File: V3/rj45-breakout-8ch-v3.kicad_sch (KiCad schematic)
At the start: 13 parts, among them J1 Jack RJ45, J10 Conn_01x06, J11 Conn_01x06, J12 Conn_01x06, J13 Conn_01x06, J2 Jack RJ45, J3 Jack RJ45, J4 Jack RJ45, J5 Jack RJ45, J6 Jack RJ45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

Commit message: Part numbers update
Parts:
- J1, J2, J3, J4, J5, J6, J7, J8: JLCPCB BOM (none) -> 0
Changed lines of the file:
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@@
       (effects (font (size 1.27 1.27)) hide)
     )
-    (property "JLCPCB BOM" "~" (at 77.47 140.97 0)
+    (property "JLCPCB BOM" "0" (at 77.47 140.97 0)
       (effects (font (size 1.27 1.27)) hide)
     )
@@
       (effects (font (size 1.27 1.27)) hide)
     )
-    (property "JLCPCB BOM" "~" (at 77.47 110.49 0)
+    (property "JLCPCB BOM" "0" (at 77.47 110.49 0)
       (effects (font (size 1.27 1.27)) hide)
     )
@@
       (effects (font (size 1.27 1.27)) hide)
     )
-    (property "JLCPCB BOM" "~" (at 77.47 80.01 0)
+    (property "JLCPCB BOM" "0" (at 77.47 80.01 0)
       (effects (font (size 1.27 1.27)) hide)
     )
@@
       (effects (font (size 1.27 1.27)) hide)
     )
-    (property "JLCPCB BOM" "~" (at 77.47 49.53 0)
+    (property "JLCPCB BOM" "0" (at 77.47 49.53 0)
       (effects (font (size 1.27 1.27)) hide)
     )
@@
       (effects (font (size 1.27 1.27)) hide)
     )
-    (property "JLCPCB BOM" "~" (at 176.53 140.97 0)
+    (property "JLCPCB BOM" "0" (at 176.53 140.97 0)
       (effects (font (size 1.27 1.27)) hide)
     )
@@
       (effects (font (size 1.27 1.27)) hide)
     )
-    (property "JLCPCB BOM" "~" (at 176.53 110.49 0)
+    (property "JLCPCB BOM" "0" (at 176.53 110.49 0)
       (effects (font (size 1.27 1.27)) hide)
     )
@@
       (effects (font (size 1.27 1.27)) hide)
     )
-    (property "JLCPCB BOM" "~" (at 176.53 80.01 0)
+    (property "JLCPCB BOM" "0" (at 176.53 80.01 0)
       (effects (font (size 1.27 1.27)) hide)
     )
@@
       (effects (font (size 1.27 1.27)) hide)
     )
-    (property "JLCPCB BOM" "~" (at 176.53 49.53 0)
-      (effects (font (size 1.27 1.27)) hide)
-    )
+    (property "JLCPCB BOM" "0" (at 176.53 49.53 0)
+      (effects (font (size 1.27 1.27)) hide)
+    )

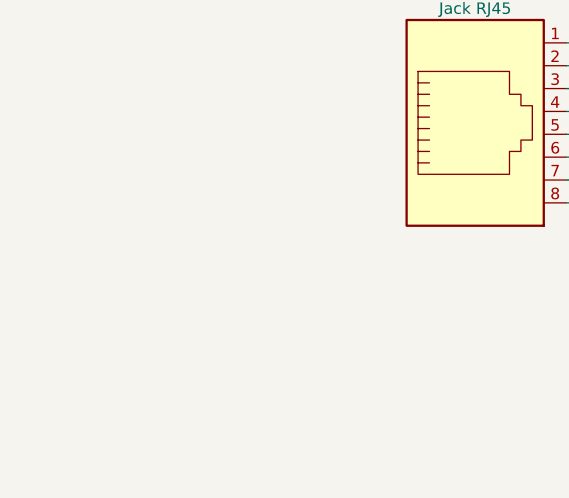
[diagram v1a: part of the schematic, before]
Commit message: Added information on RJ45 connectors
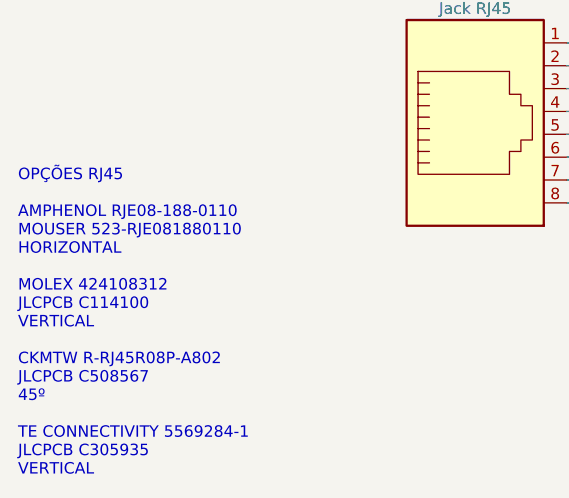
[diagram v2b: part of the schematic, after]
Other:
- note added: "OPÇÕES RJ45 AMPHENOL RJE08-188-0110 MOUSER 523-RJE081880110 HORIZONTAL MOLEX 424108312 JLCPCB C114100 VERTICAL CKMTW R-RJ45R08P-A802 JLCPCB C508567 45º TE CONNECTIVITY 5569284-1 JLCPCB C305935 VERTICAL"
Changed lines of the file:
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@@
     (stroke (width 0) (type default))
+  )
+  (text "OPÇÕES RJ45\n\nAMPHENOL RJE08-188-0110\nMOUSER 523-RJE081880110\nHORIZONTAL\n\nMOLEX 424108312\nJLCPCB C114100\nVERTICAL\n\nCKMTW R-RJ45R08P-A802\nJLCPCB C508567\n45º\n\nTE CONNECTIVITY 5569284-1\nJLCPCB C305935\nVERTICAL"
+    (at 26.67 181.61 0)
+    (effects (font (size 1.27 1.27)) (justify left bottom))
   )
   (symbol (lib_id "Connector:RJ45") (at 77.47 140.97 0) (mirror x) (unit 1)

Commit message: Connectors rotated 180deg
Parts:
- J10, J11, J12, J13: footprint Tales:TerminalBlock_DG141V-2.54-6P_1x06_P2.54mm_Vertical -> Tales:TerminalBlock_Phoenix_FFKDSA1-V-2.54-6_1x06_P2.54mm_Vertical
- J9: footprint Tales:TerminalBlock_JL142V-5.08-2P_1x02_P5.08mm_Vertical -> Tales:TerminalBlock_Phoenix_FFKDSA-V1-5.08-2_1x02_P5.08mm_Vertical
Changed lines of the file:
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@@
       (effects (font (size 1.27 1.27)) (justify left))
     )
-    (property "Footprint" "Tales:TerminalBlock_DG141V-2.54-6P_1x06_P2.54mm_Vertical" (at 212.09 64.77 0)
+    (property "Footprint" "Tales:TerminalBlock_Phoenix_FFKDSA1-V-2.54-6_1x06_P2.54mm_Vertical" (at 212.09 64.77 0)
       (effects (font (size 1.27 1.27)) hide)
     )
@@
       (effects (font (size 1.27 1.27)) (justify left))
     )
-    (property "Footprint" "Tales:TerminalBlock_DG141V-2.54-6P_1x06_P2.54mm_Vertical" (at 113.03 125.73 0)
+    (property "Footprint" "Tales:TerminalBlock_Phoenix_FFKDSA1-V-2.54-6_1x06_P2.54mm_Vertical" (at 113.03 125.73 0)
       (effects (font (size 1.27 1.27)) hide)
     )
@@
       (effects (font (size 1.27 1.27)) (justify left))
     )
-    (property "Footprint" "Tales:TerminalBlock_JL142V-5.08-2P_1x02_P5.08mm_Vertical" (at 113.03 29.21 0)
+    (property "Footprint" "Tales:TerminalBlock_Phoenix_FFKDSA-V1-5.08-2_1x02_P5.08mm_Vertical" (at 113.03 29.21 0)
       (effects (font (size 1.27 1.27)) hide)
     )
@@
       (effects (font (size 1.27 1.27)) (justify left))
     )
-    (property "Footprint" "Tales:TerminalBlock_DG141V-2.54-6P_1x06_P2.54mm_Vertical" (at 113.03 64.77 0)
+    (property "Footprint" "Tales:TerminalBlock_Phoenix_FFKDSA1-V-2.54-6_1x06_P2.54mm_Vertical" (at 113.03 64.77 0)
       (effects (font (size 1.27 1.27)) hide)
     )
@@
       (effects (font (size 1.27 1.27)) (justify left))
     )
-    (property "Footprint" "Tales:TerminalBlock_DG141V-2.54-6P_1x06_P2.54mm_Vertical" (at 212.09 125.73 0)
+    (property "Footprint" "Tales:TerminalBlock_Phoenix_FFKDSA1-V-2.54-6_1x06_P2.54mm_Vertical" (at 212.09 125.73 0)
       (effects (font (size 1.27 1.27)) hide)
     )

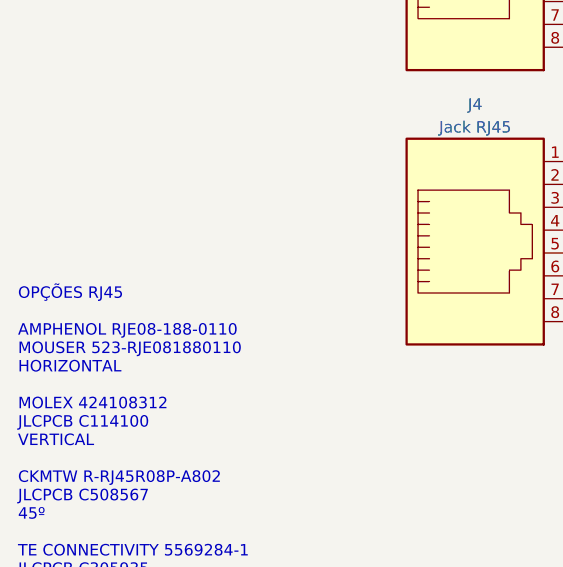
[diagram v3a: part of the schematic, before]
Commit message: Added text regarding RJ45 connectors
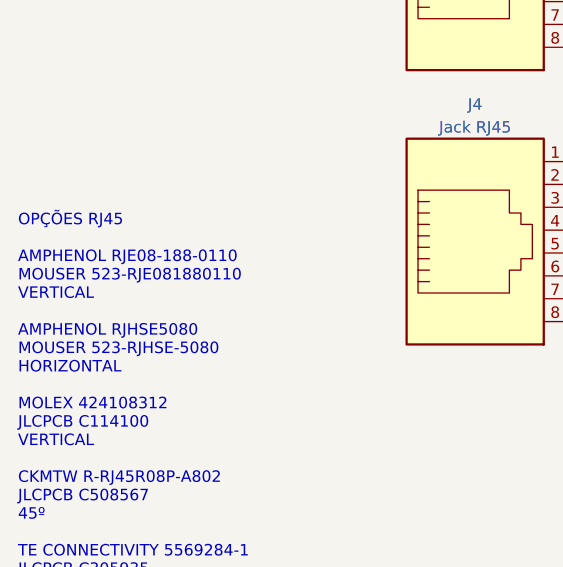
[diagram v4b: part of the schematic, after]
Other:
- note added: "OPÇÕES RJ45 AMPHENOL RJE08-188-0110 MOUSER 523-RJE081880110 VERTICAL AMPHENOL RJHSE5080 MOUSER 523-RJHSE-5080 HORIZONTAL MOLEX 424108312 JLCPCB C114100 VERTICAL CKMTW R-RJ45R08P-A802 JLCPCB C508567 45º TE CONNECTIVITY 5569284-1 JLCPCB C305935 VERTICAL"
- note removed: "OPÇÕES RJ45 AMPHENOL RJE08-188-0110 MOUSER 523-RJE081880110 HORIZONTAL MOLEX 424108312 JLCPCB C114100 VERTICAL CKMTW R-RJ45R08P-A802 JLCPCB C508567 45º TE CONNECTIVITY 5569284-1 JLCPCB C305935 VERTICAL"
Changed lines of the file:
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@@
     (stroke (width 0) (type default))
   )
-  (text "OPÇÕES RJ45\n\nAMPHENOL RJE08-188-0110\nMOUSER 523-RJE081880110\nHORIZONTAL\n\nMOLEX 424108312\nJLCPCB C114100\nVERTICAL\n\nCKMTW R-RJ45R08P-A802\nJLCPCB C508567\n45º\n\nTE CONNECTIVITY 5569284-1\nJLCPCB C305935\nVERTICAL"
+  (text "OPÇÕES RJ45\n\nAMPHENOL RJE08-188-0110\nMOUSER 523-RJE081880110\nVERTICAL\n\nAMPHENOL RJHSE5080\nMOUSER 523-RJHSE-5080\nHORIZONTAL\n\nMOLEX 424108312\nJLCPCB C114100\nVERTICAL\n\nCKMTW R-RJ45R08P-A802\nJLCPCB C508567\n45º\n\nTE CONNECTIVITY 5569284-1\nJLCPCB C305935\nVERTICAL"
     (at 26.67 181.61 0)
     (effects (font (size 1.27 1.27)) (justify left bottom))

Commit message: Layout tweakings
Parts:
- added FID1, FID2, FID3, FID4: Fiducial, Fiducial:Fiducial_1mm_Mask2mm, symbol Mechanical:Fiducial
- J1, J2, J3, J4, J5, J6, J7, J8: JLCPCB BOM 0 -> 1; LCSC Part (none) -> C2902702; Mfr Amphenol -> Ckmtw(Shenzhen Cankemeng); Mfr PN RJE08-188-0110 -> R-RJ45S08P-A004; Vendor Mouser -> JLCPCB; Vendor PN 523-RJE081880110 -> C2902702
- J10: value Conn_01x06 -> SWITCHES1; footprint Tales:TerminalBlock_Phoenix_FFKDSA1-V-2.54-6_1x06_P2.54mm_Vertical -> Tales:TerminalBlock_DB141V-2.54-6P_1x06_P2.54mm_Vertical
- J11: value Conn_01x06 -> SWITCHES2; footprint Tales:TerminalBlock_Phoenix_FFKDSA1-V-2.54-6_1x06_P2.54mm_Vertical -> Tales:TerminalBlock_DB141V-2.54-6P_1x06_P2.54mm_Vertical
- J12: value Conn_01x06 -> SWITCHES3; footprint Tales:TerminalBlock_Phoenix_FFKDSA1-V-2.54-6_1x06_P2.54mm_Vertical -> Tales:TerminalBlock_DB141V-2.54-6P_1x06_P2.54mm_Vertical
- J13: value Conn_01x06 -> SWITCHES4; footprint Tales:TerminalBlock_Phoenix_FFKDSA1-V-2.54-6_1x06_P2.54mm_Vertical -> Tales:TerminalBlock_DB141V-2.54-6P_1x06_P2.54mm_Vertical
- J9: value Conn_01x02 -> 24V; footprint Tales:TerminalBlock_Phoenix_FFKDSA-V1-5.08-2_1x02_P5.08mm_Vertical -> Tales:TerminalBlock_DB142V-2-5.08_1x02_P5.08mm_Vertical; LCSC Part C409160 -> C2898699; Mfr JILN -> DIBO; Mfr PN JL142V-50802GA1 -> DB142V-5.08-2P; Vendor PN C409160 -> C2898699
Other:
- note added: "OPÇÕES RJ45 AMPHENOL RJE08-188-0110 MOUSER 523-RJE081880110 CKMTW(Shenzhen Cankemeng) R-RJ45S08P-A004 JLCPCB C2902702"
- note removed: "OPÇÕES RJ45 AMPHENOL RJE08-188-0110 MOUSER 523-RJE081880110 VERTICAL AMPHENOL RJHSE5080 MOUSER 523-RJHSE-5080 HORIZONTAL MOLEX 424108312 JLCPCB C114100 VERTICAL CKMTW R-RJ45R08P-A802 JLCPCB C508567 45º TE CONNECTIVITY 5569284-1 JLCPCB C305935 VERTICAL"

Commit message: Footprints updated
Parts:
- removed FID1, FID2, FID3, FID4: Fiducial, Fiducial:Fiducial_1mm_Mask2mm, symbol Mechanical:Fiducial
- J1, J2, J3, J4, J5, J6, J7, J8: footprint Tales:RJ45_Amphenol_P-RJE08-188-0X10 -> Tales:RJ45_CKMTW_R-RJ45S08P-A004
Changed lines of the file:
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@@
       (effects (font (size 1.27 1.27)))
     )
-    (property "Footprint" "Tales:RJ45_Amphenol_P-RJE08-188-0X10" (at 77.47 141.605 90)
+    (property "Footprint" "Tales:RJ45_CKMTW_R-RJ45S08P-A004" (at 77.47 141.605 90)
       (effects (font (size 1.27 1.27)) hide)
     )
@@
       (effects (font (size 1.27 1.27)))
     )
-    (property "Footprint" "Tales:RJ45_Amphenol_P-RJE08-188-0X10" (at 77.47 111.125 90)
+    (property "Footprint" "Tales:RJ45_CKMTW_R-RJ45S08P-A004" (at 77.47 111.125 90)
       (effects (font (size 1.27 1.27)) hide)
     )
@@
       (effects (font (size 1.27 1.27)))
     )
-    (property "Footprint" "Tales:RJ45_Amphenol_P-RJE08-188-0X10" (at 77.47 80.645 90)
+    (property "Footprint" "Tales:RJ45_CKMTW_R-RJ45S08P-A004" (at 77.47 80.645 90)
       (effects (font (size 1.27 1.27)) hide)
     )
@@
       (effects (font (size 1.27 1.27)))
     )
-    (property "Footprint" "Tales:RJ45_Amphenol_P-RJE08-188-0X10" (at 77.47 50.165 90)
+    (property "Footprint" "Tales:RJ45_CKMTW_R-RJ45S08P-A004" (at 77.47 50.165 90)
       (effects (font (size 1.27 1.27)) hide)
     )
@@
       (effects (font (size 1.27 1.27)))
     )
-    (property "Footprint" "Tales:RJ45_Amphenol_P-RJE08-188-0X10" (at 176.53 141.605 90)
+    (property "Footprint" "Tales:RJ45_CKMTW_R-RJ45S08P-A004" (at 176.53 141.605 90)
       (effects (font (size 1.27 1.27)) hide)
     )
@@
       (effects (font (size 1.27 1.27)))
     )
-    (property "Footprint" "Tales:RJ45_Amphenol_P-RJE08-188-0X10" (at 176.53 111.125 90)
+    (property "Footprint" "Tales:RJ45_CKMTW_R-RJ45S08P-A004" (at 176.53 111.125 90)
       (effects (font (size 1.27 1.27)) hide)
     )
@@
       (effects (font (size 1.27 1.27)))
     )
-    (property "Footprint" "Tales:RJ45_Amphenol_P-RJE08-188-0X10" (at 176.53 80.645 90)
+    (property "Footprint" "Tales:RJ45_CKMTW_R-RJ45S08P-A004" (at 176.53 80.645 90)
       (effects (font (size 1.27 1.27)) hide)
     )
@@
       (effects (font (size 1.27 1.27)))
     )
-    (property "Footprint" "Tales:RJ45_Amphenol_P-RJE08-188-0X10" (at 176.53 50.165 90)
+    (property "Footprint" "Tales:RJ45_CKMTW_R-RJ45S08P-A004" (at 176.53 50.165 90)
       (effects (font (size 1.27 1.27)) hide)
     )
@@
     )
   )
-  (symbol (lib_id "Mechanical:Fiducial") (at 162.56 179.07 0) (unit 1)
-    (in_bom yes) (on_board yes) (dnp no) (fields_autoplaced)
-    (property "Reference" "FID3" (at 165.1 178.435 0)
-      (effects (font (size 1.27 1.27)) (justify left))
-    )
-    (property "Value" "Fiducial" (at 165.1 180.975 0)
-      (effects (font (size 1.27 1.27)) (justify left))
-    )
-    (property "Footprint" "Fiducial:Fiducial_1mm_Mask2mm" (at 162.56 179.07 0)
-      (effects (font (size 1.27 1.27)) hide)
-    )
-    (property "Datasheet" "~" (at 162.56 179.07 0)
-      (effects (font (size 1.27 1.27)) hide)
-    )
-    (instances
-      (project "rj45-breakout-8ch-v3"
-        (path "/e63e39d7-6ac0-4ffd-8aa3-1841a4541b55"
-          (reference "FID3") (unit 1)
-        )
-      )
-    )
-  )
-  (symbol (lib_id "Mechanical:Fiducial") (at 162.56 186.69 0) (unit 1)
-    (in_bom yes) (on_board yes) (dnp no) (fields_autoplaced)
-    (property "Reference" "FID2" (at 165.1 186.055 0)
-      (effects (font (size 1.27 1.27)) (justify left))
-    )
-    (property "Value" "Fiducial" (at 165.1 188.595 0)
-      (effects (font (size 1.27 1.27)) (justify left))
-    )
-    (property "Footprint" "Fiducial:Fiducial_1mm_Mask2mm" (at 162.56 186.69 0)
-      (effects (font (size 1.27 1.27)) hide)
-    )
-    (property "Datasheet" "~" (at 162.56 186.69 0)
-      (effects (font (size 1.27 1.27)) hide)
-    )
-    (instances
-      (project "rj45-breakout-8ch-v3"
-        (path "/e63e39d7-6ac0-4ffd-8aa3-1841a4541b55"
-          (reference "FID2") (unit 1)
-        )
-      )
-    )
-  )
-  (symbol (lib_id "Mechanical:Fiducial") (at 162.56 193.04 0) (unit 1)
-    (in_bom yes) (on_board yes) (dnp no) (fields_autoplaced)
-    (property "Reference" "FID1" (at 165.1 192.405 0)
-      (effects (font (size 1.27 1.27)) (justify left))
-    )
-    (property "Value" "Fiducial" (at 165.1 194.945 0)
-      (effects (font (size 1.27 1.27)) (justify left))
-    )
-    (property "Footprint" "Fiducial:Fiducial_1mm_Mask2mm" (at 162.56 193.04 0)
-      (effects (font (size 1.27 1.27)) hide)
-    )
-    (property "Datasheet" "~" (at 162.56 193.04 0)
-      (effects (font (size 1.27 1.27)) hide)
-    )
-    (instances
-      (project "rj45-breakout-8ch-v3"
-        (path "/e63e39d7-6ac0-4ffd-8aa3-1841a4541b55"
-          (reference "FID1") (unit 1)
-        )
-      )
-    )
-  )
   (symbol (lib_id "Connector_Generic:Conn_01x02") (at 113.03 29.21 0) (unit 1)
     (in_bom yes) (on_board yes) (dnp no) (fields_autoplaced)
@@
         )
       )
-    )
-  )
-  (symbol (lib_id "Mechanical:Fiducial") (at 162.56 171.45 0) (unit 1)
-    (in_bom yes) (on_board yes) (dnp no) (fields_autoplaced)
-    (property "Reference" "FID4" (at 165.1 170.815 0)
-      (effects (font (size 1.27 1.27)) (justify left))
-    )
-    (property "Value" "Fiducial" (at 165.1 173.355 0)
-      (effects (font (size 1.27 1.27)) (justify left))
-    )
-    (property "Footprint" "Fiducial:Fiducial_1mm_Mask2mm" (at 162.56 171.45 0)
-      (effects (font (size 1.27 1.27)) hide)
-    )
-    (property "Datasheet" "~" (at 162.56 171.45 0)
-      (effects (font (size 1.27 1.27)) hide)
-    )
-    (instances
-      (project "rj45-breakout-8ch-v3"
-        (path "/e63e39d7-6ac0-4ffd-8aa3-1841a4541b55"
-          (reference "FID4") (unit 1)
-        )
-      )

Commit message: Bla
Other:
- note added: "OPÇÕES RJ45 VERTICAL AMPHENOL RJE08-188-0110 MOUSER 523-RJE081880110 CKMTW(Shenzhen Cankemeng) R-RJ45S08P-A004 JLCPCB C2902702"
- note removed: "OPÇÕES RJ45 AMPHENOL RJE08-188-0110 MOUSER 523-RJE081880110 CKMTW(Shenzhen Cankemeng) R-RJ45S08P-A004 JLCPCB C2902702"
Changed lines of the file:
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@@
     (stroke (width 0) (type default))
   )
-  (text "OPÇÕES RJ45\n\nAMPHENOL RJE08-188-0110\nMOUSER 523-RJE081880110\n\nCKMTW(Shenzhen Cankemeng) R-RJ45S08P-A004\nJLCPCB C2902702"
+  (text "OPÇÕES RJ45 VERTICAL\n\nAMPHENOL RJE08-188-0110\nMOUSER 523-RJE081880110\n\nCKMTW(Shenzhen Cankemeng) R-RJ45S08P-A004\nJLCPCB C2902702"
     (at 26.67 176.53 0)
     (effects (font (size 1.27 1.27)) (justify left bottom))

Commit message: Cosmetic enhancements to PCB
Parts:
- J10: value SWITCHES1 -> DB141V-2.54-6P; footprint Tales:TerminalBlock_DB141V-2.54-6P_1x06_P2.54mm_Vertical -> Tales:TerminalBlock_Dibo_DB141V-2.54-6P_1x06_P2.54mm_Vertical
- J11: value SWITCHES2 -> DB141V-2.54-6P; footprint Tales:TerminalBlock_DB141V-2.54-6P_1x06_P2.54mm_Vertical -> Tales:TerminalBlock_Dibo_DB141V-2.54-6P_1x06_P2.54mm_Vertical
- J12: value SWITCHES3 -> DB141V-2.54-6P; footprint Tales:TerminalBlock_DB141V-2.54-6P_1x06_P2.54mm_Vertical -> Tales:TerminalBlock_Dibo_DB141V-2.54-6P_1x06_P2.54mm_Vertical
- J13: value SWITCHES4 -> DB141V-2.54-6P; footprint Tales:TerminalBlock_DB141V-2.54-6P_1x06_P2.54mm_Vertical -> Tales:TerminalBlock_Dibo_DB141V-2.54-6P_1x06_P2.54mm_Vertical
- J9: value 24V -> DB142V-5.08-2P; footprint Tales:TerminalBlock_DB142V-2-5.08_1x02_P5.08mm_Vertical -> Tales:TerminalBlock_Dibo_DB142V-2-5.08_1x02_P5.08mm_Vertical
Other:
- note added: "+24V"
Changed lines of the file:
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@@
+    (effects (font (size 1.27 1.27)) (justify left bottom))
+  )
+  (text "+24V" (at 110.49 26.67 0)
     (effects (font (size 1.27 1.27)) (justify left bottom))
   )
@@
       (effects (font (size 1.27 1.27)) (justify left))
     )
-    (property "Value" "SWITCHES3" (at 214.63 67.945 0)
-      (effects (font (size 1.27 1.27)) (justify left))
-    )
-    (property "Footprint" "Tales:TerminalBlock_DB141V-2.54-6P_1x06_P2.54mm_Vertical" (at 212.09 64.77 0)
+    (property "Value" "DB141V-2.54-6P" (at 214.63 67.945 0)
+      (effects (font (size 1.27 1.27)) (justify left))
+    )
+    (property "Footprint" "Tales:TerminalBlock_Dibo_DB141V-2.54-6P_1x06_P2.54mm_Vertical" (at 212.09 64.77 0)
       (effects (font (size 1.27 1.27)) hide)
     )
@@
       (effects (font (size 1.27 1.27)) (justify left))
     )
-    (property "Value" "SWITCHES2" (at 115.57 128.905 0)
-      (effects (font (size 1.27 1.27)) (justify left))
-    )
-    (property "Footprint" "Tales:TerminalBlock_DB141V-2.54-6P_1x06_P2.54mm_Vertical" (at 113.03 125.73 0)
+    (property "Value" "DB141V-2.54-6P" (at 115.57 128.905 0)
+      (effects (font (size 1.27 1.27)) (justify left))
+    )
+    (property "Footprint" "Tales:TerminalBlock_Dibo_DB141V-2.54-6P_1x06_P2.54mm_Vertical" (at 113.03 125.73 0)
       (effects (font (size 1.27 1.27)) hide)
     )
@@
       (effects (font (size 1.27 1.27)) (justify left))
     )
-    (property "Value" "24V" (at 115.57 32.385 0)
-      (effects (font (size 1.27 1.27)) (justify left))
-    )
-    (property "Footprint" "Tales:TerminalBlock_DB142V-2-5.08_1x02_P5.08mm_Vertical" (at 113.03 29.21 0)
+    (property "Value" "DB142V-5.08-2P" (at 115.57 32.385 0)
+      (effects (font (size 1.27 1.27)) (justify left))
+    )
+    (property "Footprint" "Tales:TerminalBlock_Dibo_DB142V-2-5.08_1x02_P5.08mm_Vertical" (at 113.03 29.21 0)
       (effects (font (size 1.27 1.27)) hide)
     )
@@
       (effects (font (size 1.27 1.27)) (justify left))
     )
-    (property "Value" "SWITCHES1" (at 115.57 67.945 0)
-      (effects (font (size 1.27 1.27)) (justify left))
-    )
-    (property "Footprint" "Tales:TerminalBlock_DB141V-2.54-6P_1x06_P2.54mm_Vertical" (at 113.03 64.77 0)
+    (property "Value" "DB141V-2.54-6P" (at 115.57 67.945 0)
+      (effects (font (size 1.27 1.27)) (justify left))
+    )
+    (property "Footprint" "Tales:TerminalBlock_Dibo_DB141V-2.54-6P_1x06_P2.54mm_Vertical" (at 113.03 64.77 0)
       (effects (font (size 1.27 1.27)) hide)
     )
@@
       (effects (font (size 1.27 1.27)) (justify left))
     )
-    (property "Value" "SWITCHES4" (at 214.63 128.905 0)
-      (effects (font (size 1.27 1.27)) (justify left))
-    )
-    (property "Footprint" "Tales:TerminalBlock_DB141V-2.54-6P_1x06_P2.54mm_Vertical" (at 212.09 125.73 0)
-      (effects (font (size 1.27 1.27)) hide)
-    )
+    (property "Value" "DB141V-2.54-6P" (at 214.63 128.905 0)
+      (effects (font (size 1.27 1.27)) (justify left))
+    )
+    (property "Footprint" "Tales:TerminalBlock_Dibo_DB141V-2.54-6P_1x06_P2.54mm_Vertical" (at 212.09 125.73 0)
+      (effects (font (size 1.27 1.27)) hide)
+    )
